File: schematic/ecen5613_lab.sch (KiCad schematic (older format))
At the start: 20 parts, among them Q1 2N2907, SW3 Bootloader, U1 AT89C51RC2, U3 74LS373, U4 bq4011YMA-100, U6 ATF16V8C, Y1 11.0592MHz

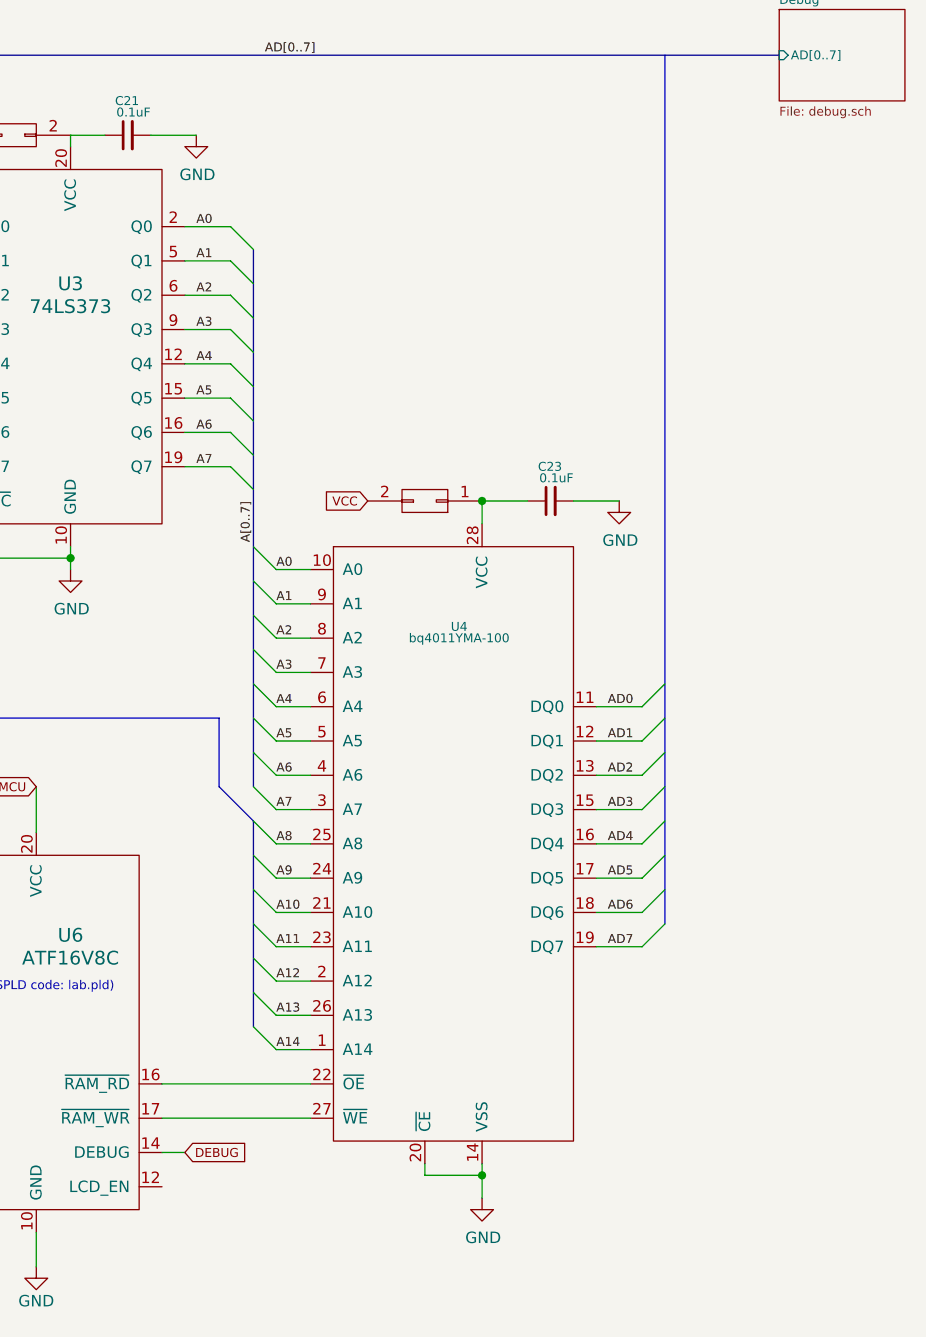
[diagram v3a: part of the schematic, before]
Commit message: [L4] Add LCD to schematic
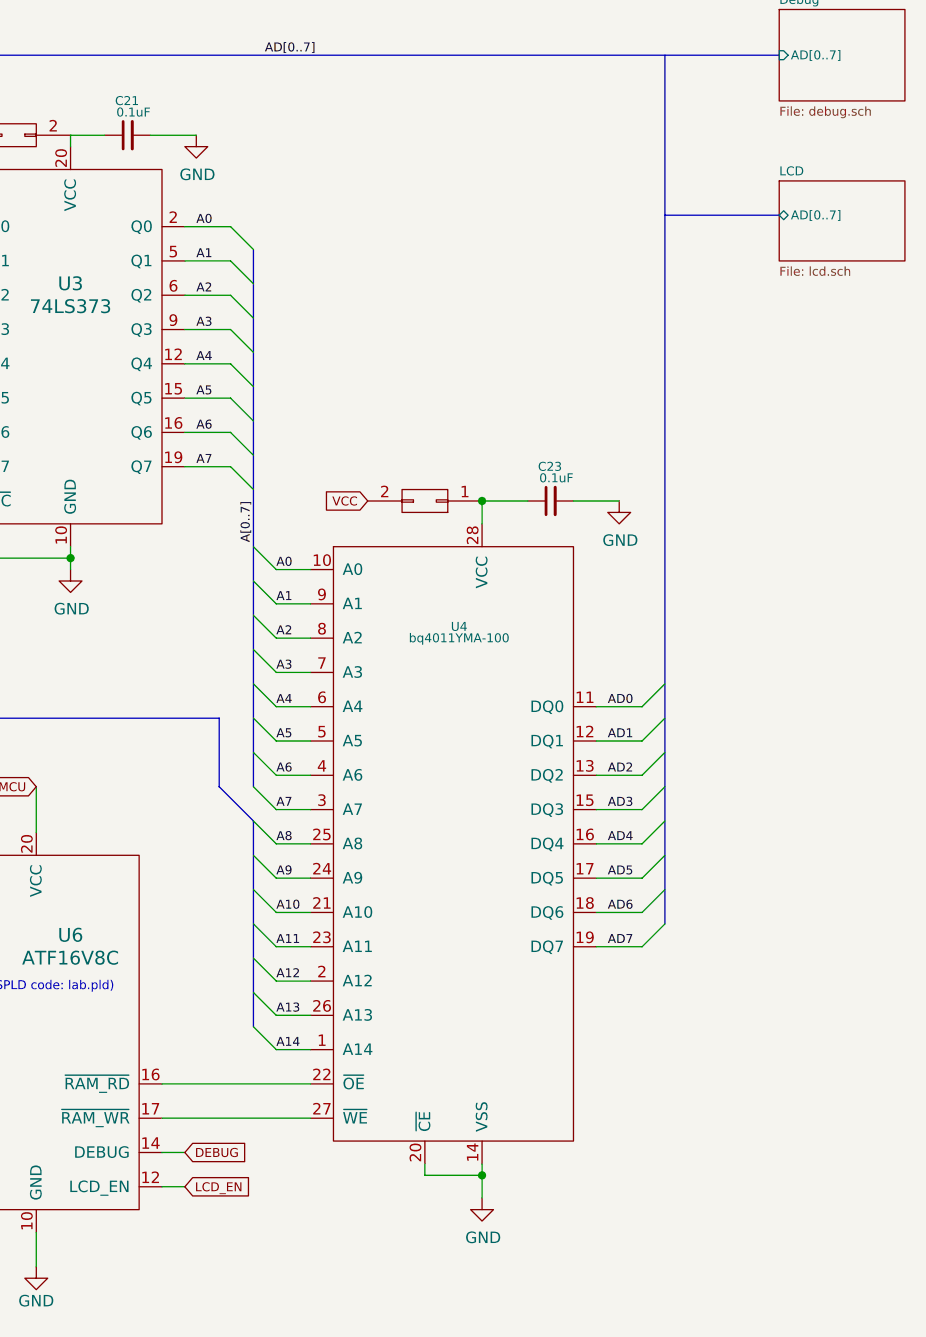
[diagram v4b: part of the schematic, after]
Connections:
- net LCD_EN: now reaches U6.12 (LCD_EN)
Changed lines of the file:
@@
 $Descr USLetter 11000 8500
 encoding utf-8
-Sheet 1 4
+Sheet 1 5
 Title "ECEN5613 Lab"
 Date "F2017"
@@
 Wire Wire Line
 	6950 6150 6300 6150
+Text GLabel 6400 6450 2    39   Input ~ 0
+LCD_EN
+Wire Wire Line
+	6400 6450 6300 6450
+$Sheet
+S 9000 2050 550  350
+U 5A001753
+F0 "LCD" 39
+F1 "lcd.sch" 39
+F2 "AD[0..7]" B L 9000 2200 39
+$EndSheet
+Wire Bus Line
+	8500 2200 9000 2200
 $EndSCHEMATC

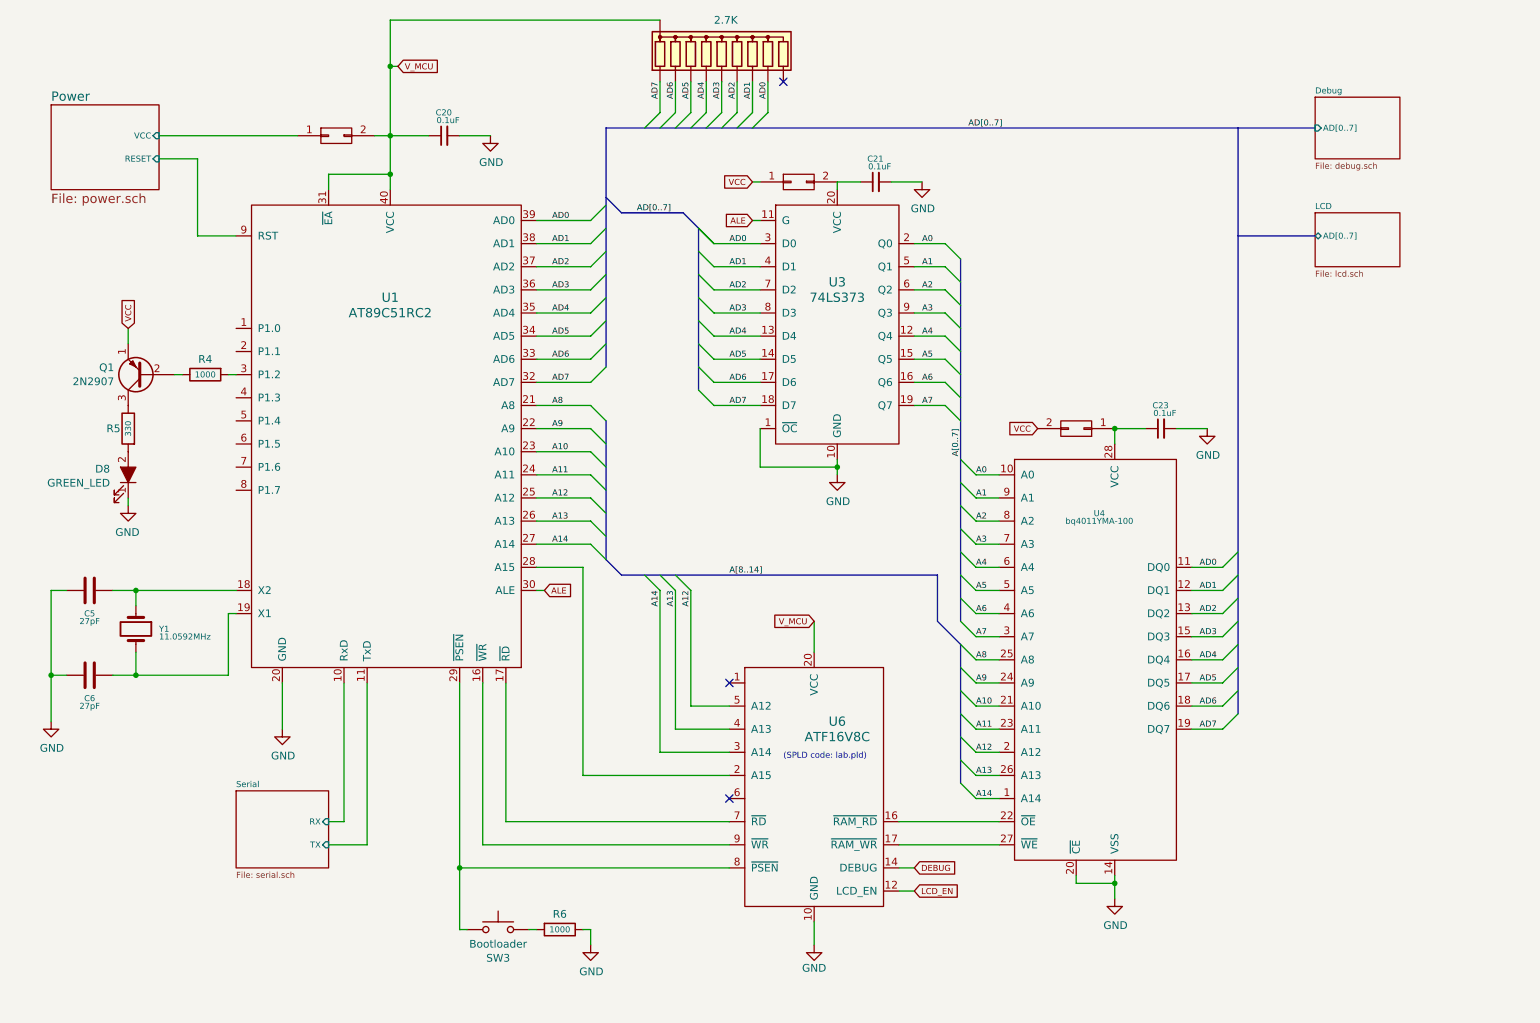
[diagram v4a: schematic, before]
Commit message: [L4] Add EEPROM to schematic
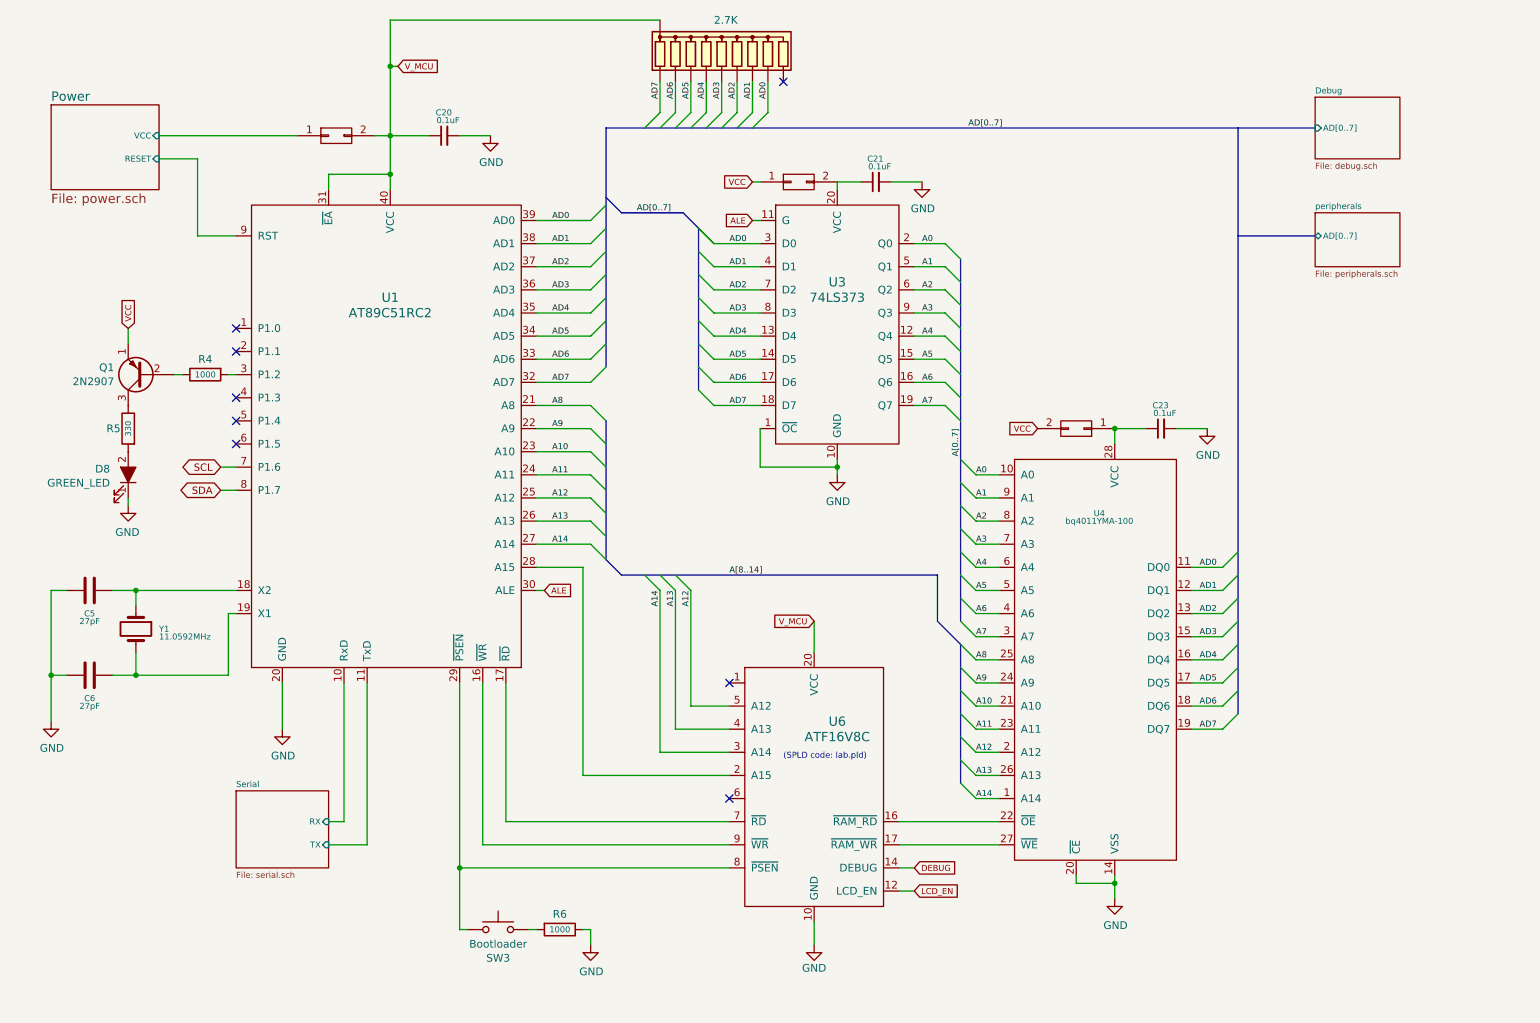
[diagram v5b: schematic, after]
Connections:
- net SCL: now reaches U1.7 (P1.6)
- net SDA: now reaches U1.8 (P1.7)
- no-connect marks 3 -> 8
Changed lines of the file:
@@
 S 9000 2050 550  350
 U 5A001753
-F0 "LCD" 39
-F1 "lcd.sch" 39
+F0 "peripherals" 39
+F1 "peripherals.sch" 39
 F2 "AD[0..7]" B L 9000 2200 39
 $EndSheet
 Wire Bus Line
 	8500 2200 9000 2200
+Text GLabel 1900 3700 0    47   BiDi ~ 0
+SCL
+Text GLabel 1900 3850 0    47   BiDi ~ 0
+SDA
+Wire Wire Line
+	1900 3700 2000 3700
+Wire Wire Line
+	1900 3850 2000 3850
+NoConn ~ 2000 3550
+NoConn ~ 2000 3400
+NoConn ~ 2000 3250
+NoConn ~ 2000 2950
+NoConn ~ 2000 2800
 $EndSCHEMATC

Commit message: [L4] Add I/O expander to schematic
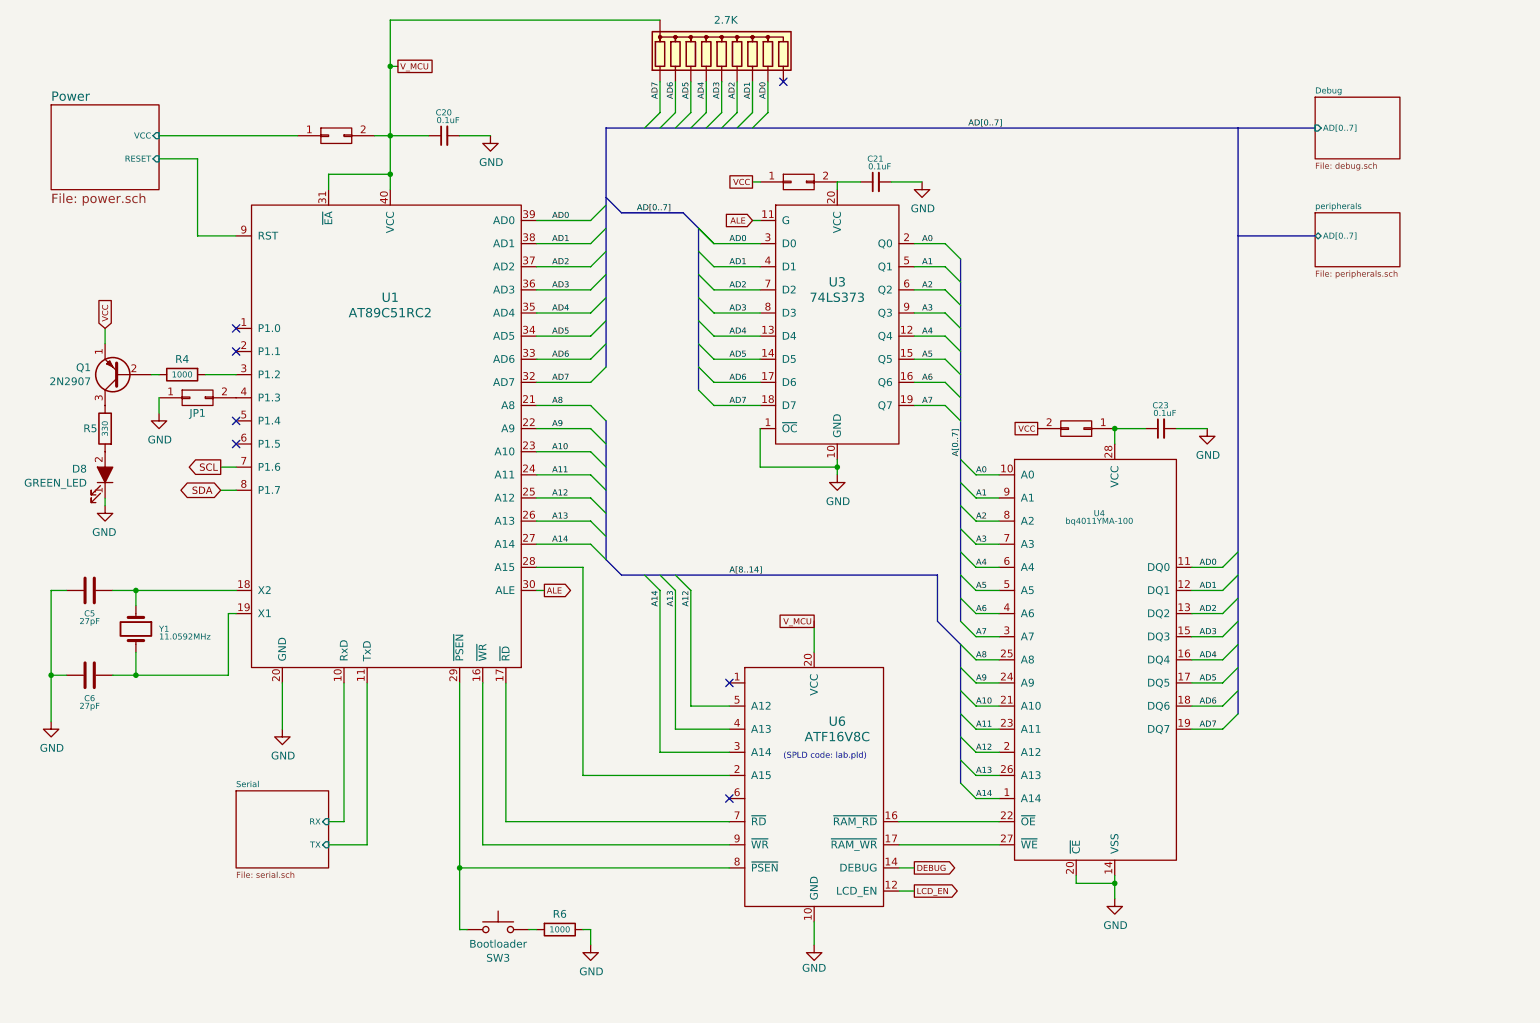
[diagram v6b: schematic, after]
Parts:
- added JP1: CONN_02X01, symbol CONN_02X01
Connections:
- net GND: now also JP1.1 (P1)
- net at U1.4 (P1.3): now also JP1.2 (P2)
- no-connect marks 8 -> 7
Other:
- moved on the sheet: D8, Q1, R4, R5
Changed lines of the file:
@@
 LIBS:interface
 LIBS:digital-audio
-LIBS:philips
 LIBS:display
 LIBS:cypress
@@
 	-1   0    0    1
 $EndComp
-Text GLabel 7200 3450 0    39   Input ~ 0
+Text GLabel 7200 3450 0    39   UnSpc ~ 0
 VCC
 $Comp
@@
 	1    0    0    -1
 $EndComp
-Text GLabel 4000 4500 2    39   Input ~ 0
+Text GLabel 4000 4500 2    39   Output ~ 0
 ALE
 Text GLabel 5350 2100 0    39   Input ~ 0
@@
 	1    0    0    -1
 $EndComp
-Text GLabel 5750 4700 0    39   Input ~ 0
+Text GLabel 5750 4700 0    39   UnSpc ~ 0
 V_MCU
 $Sheet
@@
 L Q_PNP_EBC Q1
 U 1 1 59CE0FA5
-P 1400 3100
-F 0 "Q1" H 1591 3054 50  0000 L CNN
-F 1 "2N2907" H 1591 3145 50  0000 L CNN
-F 2 "" H 1600 3200 50  0001 C CNN
-F 3 "" H 1400 3100 50  0001 C CNN
-	1    1400 3100
+P 1250 3100
+F 0 "Q1" H 1441 3054 50  0000 L CNN
+F 1 "2N2907" H 1441 3145 50  0000 L CNN
+F 2 "" H 1450 3200 50  0001 C CNN
+F 3 "" H 1250 3100 50  0001 C CNN
+	1    1250 3100
 	-1   0    0    1
 $EndComp
@@
 L R R5
 U 1 1 59CE0FA6
-P 1300 3450
-F 0 "R5" H 1350 3450 50  0000 L CNN
-F 1 "330" V 1300 3450 39  0000 C CNN
-F 2 "" V 1230 3450 50  0001 C CNN
-F 3 "" H 1300 3450 50  0001 C CNN
-	1    1300 3450
+P 1150 3450
+F 0 "R5" H 1200 3450 50  0000 L CNN
+F 1 "330" V 1150 3450 39  0000 C CNN
+F 2 "" V 1080 3450 50  0001 C CNN
+F 3 "" H 1150 3450 50  0001 C CNN
+	1    1150 3450
 	-1   0    0    -1
 $EndComp
@@
 L R R4
 U 1 1 59CE0FA7
-P 1800 3100
-F 0 "R4" V 1700 3100 50  0000 C CNN
-F 1 "1000" V 1800 3100 39  0000 C CNN
-F 2 "" V 1730 3100 50  0001 C CNN
-F 3 "" H 1800 3100 50  0001 C CNN
-	1    1800 3100
+P 1650 3100
+F 0 "R4" V 1550 3100 50  0000 C CNN
+F 1 "1000" V 1650 3100 39  0000 C CNN
+F 2 "" V 1580 3100 50  0001 C CNN
+F 3 "" H 1650 3100 50  0001 C CNN
+	1    1650 3100
 	0    -1   1    0
 $EndComp
@@
 L LED_ALT D8
 U 1 1 59CE0FA8
-P 1300 3750
-F 0 "D8" V 1338 3632 50  0000 R CNN
-F 1 "GREEN_LED" V 1247 3632 50  0000 R CNN
-F 2 "" H 1300 3750 50  0001 C CNN
-F 3 "" H 1300 3750 50  0001 C CNN
-	1    1300 3750
+P 1150 3750
+F 0 "D8" V 1188 3632 50  0000 R CNN
+F 1 "GREEN_LED" V 1097 3632 50  0000 R CNN
+F 2 "" H 1150 3750 50  0001 C CNN
+F 3 "" H 1150 3750 50  0001 C CNN
+	1    1150 3750
 	0    1    -1   0
 $EndComp
-Text GLabel 1300 2800 1    39   Input ~ 0
+Text GLabel 1150 2800 1    39   Input ~ 0
 VCC
 $Comp
 L GND #PWR06
 U 1 1 59CE0FA9
-P 1300 3950
-F 0 "#PWR06" H 1300 3700 50  0001 C CNN
-F 1 "GND" H 1305 3777 50  0000 C CNN
-F 2 "" H 1300 3950 50  0001 C CNN
-F 3 "" H 1300 3950 50  0001 C CNN
-	1    1300 3950
+P 1150 3950
+F 0 "#PWR06" H 1150 3700 50  0001 C CNN
+F 1 "GND" H 1155 3777 50  0000 C CNN
+F 2 "" H 1150 3950 50  0001 C CNN
+F 3 "" H 1150 3950 50  0001 C CNN
+	1    1150 3950
 	-1   0    0    -1
 $EndComp
@@
 	1    0    0    -1
 $EndComp
-Text GLabel 3050 1100 2    39   Input ~ 0
+Text GLabel 3050 1100 2    39   UnSpc ~ 0
 V_MCU
 Entry Wire Line
@@
 	1    0    0    -1
 $EndComp
-Text GLabel 5350 1850 0    39   Input ~ 0
+Text GLabel 5350 1850 0    39   UnSpc ~ 0
 VCC
 $Comp
@@
 Connection ~ 1350 5050
 Wire Wire Line
-	1300 2900 1300 2800
-Wire Wire Line
-	1300 3900 1300 3950
+	1150 2900 1150 2800
+Wire Wire Line
+	1150 3900 1150 3950
 Wire Wire Line
 	3950 2100 4300 2100
@@
 Wire Bus Line
 	4500 2050 4400 1950
-Text GLabel 6400 6300 2    39   Input ~ 0
+Text GLabel 6400 6300 2    39   Output ~ 0
 DEBUG
 Wire Wire Line
@@
 $EndSheet
 Wire Wire Line
-	1650 3100 1600 3100
+	1500 3100 1450 3100
 $Comp
 L AT89C51RC2 U1
@@
 $EndComp
 Wire Wire Line
-	1950 3100 2000 3100
+	1800 3100 2000 3100
 Wire Wire Line
 	2600 1900 2600 1800
@@
 Wire Wire Line
 	6950 6150 6300 6150
-Text GLabel 6400 6450 2    39   Input ~ 0
+Text GLabel 6400 6450 2    39   Output ~ 0
 LCD_EN
 Wire Wire Line
@@
 Wire Bus Line
 	8500 2200 9000 2200
-Text GLabel 1900 3700 0    47   BiDi ~ 0
+Text GLabel 1900 3700 0    47   Output ~ 0
 SCL
 Text GLabel 1900 3850 0    47   BiDi ~ 0
@@
 NoConn ~ 2000 3550
 NoConn ~ 2000 3400
-NoConn ~ 2000 3250
 NoConn ~ 2000 2950
 NoConn ~ 2000 2800
+$Comp
+L CONN_02X01 JP1
+U 1 1 5A092DF4
+P 1750 3250
+F 0 "JP1" H 1750 3150 50  0000 C CNN
+F 1 "CONN_02X01" H 1750 3374 50  0001 C CNN
+F 2 "" H 1750 2050 50  0001 C CNN
+F 3 "" H 1750 2050 50  0001 C CNN
+	1    1750 3250
+	1    0    0    -1
+$EndComp
+$Comp
+L GND #PWR?
+U 1 1 5A093004
+P 1500 3350
+F 0 "#PWR?" H 1500 3100 50  0001 C CNN
+F 1 "GND" H 1505 3177 50  0000 C CNN
+F 2 "" H 1500 3350 50  0001 C CNN
+F 3 "" H 1500 3350 50  0001 C CNN
+	1    1500 3350
+	1    0    0    -1
+$EndComp
+Wire Wire Line
+	1500 3250 1500 3350
 $EndSCHEMATC
